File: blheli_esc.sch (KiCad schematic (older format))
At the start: 42 parts, among them J1 Conn_01x03_Male, Q1 BC847, Q2 BC847, Q3 BC847, U1 AP1509, U2 EFM8BB21F16G

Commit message: first draft complete
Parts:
- added TP6: PHASE_A, TestPoint:TestPoint_Pad_1.5x1.5mm, symbol Connector:TestPoint
- added TP7: PHASE_B, TestPoint:TestPoint_Pad_1.5x1.5mm, symbol Connector:TestPoint
- added TP8: PHASE_C, TestPoint:TestPoint_Pad_1.5x1.5mm, symbol Connector:TestPoint
- J1: footprint Connector:FanPinHeader_1x03_P2.54mm_Vertical -> Connector_PinHeader_2.54mm:PinHeader_1x03_P2.54mm_Vertical
- L1: footprint Inductor_SMD:L_12x12mm_H4.5mm -> blheli_esc:inductor_3x3mm
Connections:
- net PHASE_A: now also TP6.1
- net PHASE_B: now also TP7.1
- net PHASE_C: now also TP8.1
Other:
- moved on the sheet: J1, TP1, TP2, TP3, TP4, TP5
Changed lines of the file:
@@
 EESchema Schematic File Version 4
+LIBS:blheli_esc-cache
 EELAYER 26 0
 EELAYER END
@@
 Wire Wire Line
 	9850 1400 9850 1500
-Text GLabel 10700 1300 2    50   Output ~ 0
+Text GLabel 2850 4650 0    50   Input ~ 0
 PHASE_A
 Connection ~ 9850 1300
@@
 F 0 "L1" V 5822 1400 50  0000 C CNN
 F 1 "47uH" V 5913 1400 50  0000 C CNN
-F 2 "Inductor_SMD:L_12x12mm_H4.5mm" H 6000 1400 50  0001 C CNN
+F 2 "blheli_esc:inductor_3x3mm" H 6000 1400 50  0001 C CNN
 F 3 "~" H 6000 1400 50  0001 C CNN
 	1    6000 1400
@@
 L Connector:TestPoint TP2
 U 1 1 5C2EF43A
+P 3050 3600
+F 0 "TP2" V 3004 3787 50  0000 L CNN
+F 1 "C2CK" V 3095 3787 50  0000 L CNN
+F 2 "TestPoint:TestPoint_THTPad_D1.0mm_Drill0.5mm" H 3250 3600 50  0001 C CNN
+F 3 "~" H 3250 3600 50  0001 C CNN
+	1    3050 3600
+	0    1    1    0
+$EndComp
+Text GLabel 2850 3600 0    50   Input ~ 0
+C2CK
+Wire Wire Line
+	2850 3600 3050 3600
+$Comp
+L Connector:TestPoint TP3
+U 1 1 5C2F3D95
+P 3050 3800
+F 0 "TP3" V 3004 3987 50  0000 L CNN
+F 1 "C2D" V 3095 3987 50  0000 L CNN
+F 2 "TestPoint:TestPoint_THTPad_D1.0mm_Drill0.5mm" H 3250 3800 50  0001 C CNN
+F 3 "~" H 3250 3800 50  0001 C CNN
+	1    3050 3800
+	0    1    1    0
+$EndComp
+Text GLabel 2850 3800 0    50   Input ~ 0
+C2D
+Wire Wire Line
+	2850 3800 3050 3800
+Text GLabel 2850 4000 0    50   Input ~ 0
+TX2
+$Comp
+L Connector:TestPoint TP4
+U 1 1 5C2F885D
+P 3050 4000
+F 0 "TP4" V 3004 4188 50  0000 L CNN
+F 1 "TX2" V 3095 4188 50  0000 L CNN
+F 2 "TestPoint:TestPoint_THTPad_D1.0mm_Drill0.5mm" H 3250 4000 50  0001 C CNN
+F 3 "~" H 3250 4000 50  0001 C CNN
+	1    3050 4000
+	0    1    1    0
+$EndComp
+Wire Wire Line
+	2850 4000 3050 4000
+Text GLabel 2850 4200 0    50   Output ~ 0
+RC_IN
+$Comp
+L Connector:TestPoint TP5
+U 1 1 5C2FD85C
 P 3050 4200
-F 0 "TP2" V 3004 4387 50  0000 L CNN
-F 1 "C2CK" V 3095 4387 50  0000 L CNN
+F 0 "TP5" V 3004 4387 50  0000 L CNN
+F 1 "RC_IN" V 3095 4387 50  0000 L CNN
 F 2 "TestPoint:TestPoint_THTPad_D1.0mm_Drill0.5mm" H 3250 4200 50  0001 C CNN
 F 3 "~" H 3250 4200 50  0001 C CNN
@@
 	0    1    1    0
 $EndComp
-Text GLabel 2850 4200 0    50   Input ~ 0
-C2CK
 Wire Wire Line
 	2850 4200 3050 4200
-$Comp
-L Connector:TestPoint TP3
-U 1 1 5C2F3D95
-P 3050 4400
-F 0 "TP3" V 3004 4587 50  0000 L CNN
-F 1 "C2D" V 3095 4587 50  0000 L CNN
-F 2 "TestPoint:TestPoint_THTPad_D1.0mm_Drill0.5mm" H 3250 4400 50  0001 C CNN
-F 3 "~" H 3250 4400 50  0001 C CNN
-	1    3050 4400
-	0    1    1    0
-$EndComp
-Text GLabel 2850 4400 0    50   Input ~ 0
-C2D
-Wire Wire Line
-	2850 4400 3050 4400
-Text GLabel 2850 4600 0    50   Input ~ 0
-TX2
-$Comp
-L Connector:TestPoint TP4
-U 1 1 5C2F885D
-P 3050 4600
-F 0 "TP4" V 3004 4788 50  0000 L CNN
-F 1 "TX2" V 3095 4788 50  0000 L CNN
-F 2 "TestPoint:TestPoint_THTPad_D1.0mm_Drill0.5mm" H 3250 4600 50  0001 C CNN
-F 3 "~" H 3250 4600 50  0001 C CNN
-	1    3050 4600
-	0    1    1    0
-$EndComp
-Wire Wire Line
-	2850 4600 3050 4600
-Text GLabel 2850 4800 0    50   Output ~ 0
-RC_IN
-$Comp
-L Connector:TestPoint TP5
-U 1 1 5C2FD85C
-P 3050 4800
-F 0 "TP5" V 3004 4987 50  0000 L CNN
-F 1 "RC_IN" V 3095 4987 50  0000 L CNN
-F 2 "TestPoint:TestPoint_THTPad_D1.0mm_Drill0.5mm" H 3250 4800 50  0001 C CNN
-F 3 "~" H 3250 4800 50  0001 C CNN
-	1    3050 4800
-	0    1    1    0
-$EndComp
-Wire Wire Line
-	2850 4800 3050 4800
 $Comp
 L Connector:Conn_01x03_Male J1
 U 1 1 5C302F31
-P 1200 4400
-F 0 "J1" H 1306 4678 50  0000 C CNN
-F 1 "Conn_01x03_Male" H 1306 4587 50  0000 C CNN
-F 2 "Connector:FanPinHeader_1x03_P2.54mm_Vertical" H 1200 4400 50  0001 C CNN
-F 3 "~" H 1200 4400 50  0001 C CNN
-	1    1200 4400
+P 1200 3800
+F 0 "J1" H 1306 4078 50  0000 C CNN
+F 1 "Conn_01x03_Male" H 1306 3987 50  0000 C CNN
+F 2 "Connector_PinHeader_2.54mm:PinHeader_1x03_P2.54mm_Vertical" H 1200 3800 50  0001 C CNN
+F 3 "~" H 1200 3800 50  0001 C CNN
+	1    1200 3800
 	1    0    0    -1
 $EndComp
@@
 L power:GND #PWR0112
 U 1 1 5C30CB8C
-P 1500 4600
-F 0 "#PWR0112" H 1500 4350 50  0001 C CNN
-F 1 "GND" H 1505 4427 50  0000 C CNN
-F 2 "" H 1500 4600 50  0001 C CNN
-F 3 "" H 1500 4600 50  0001 C CNN
-	1    1500 4600
-	1    0    0    -1
-$EndComp
-Wire Wire Line
-	1400 4500 1500 4500
-Text GLabel 1600 4300 2    50   Output ~ 0
+P 1500 4000
+F 0 "#PWR0112" H 1500 3750 50  0001 C CNN
+F 1 "GND" H 1505 3827 50  0000 C CNN
+F 2 "" H 1500 4000 50  0001 C CNN
+F 3 "" H 1500 4000 50  0001 C CNN
+	1    1500 4000
+	1    0    0    -1
+$EndComp
+Wire Wire Line
+	1400 3900 1500 3900
+Text GLabel 1600 3700 2    50   Output ~ 0
 RC_IN
 Wire Wire Line
-	1400 4300 1600 4300
+	1400 3700 1600 3700
 $Comp
 L Connector:TestPoint TP1
 U 1 1 5C32EFFC
-P 1400 4400
-F 0 "TP1" V 1354 4587 50  0000 L CNN
-F 1 "SERVO_TP" V 1445 4587 50  0000 L CNN
-F 2 "TestPoint:TestPoint_THTPad_D1.0mm_Drill0.5mm" H 1600 4400 50  0001 C CNN
-F 3 "~" H 1600 4400 50  0001 C CNN
-	1    1400 4400
-	0    1    1    0
-$EndComp
-Wire Wire Line
-	1500 4600 1500 4500
+P 1400 3800
+F 0 "TP1" V 1354 3987 50  0000 L CNN
+F 1 "SERVO_TP" V 1445 3987 50  0000 L CNN
+F 2 "TestPoint:TestPoint_THTPad_D1.0mm_Drill0.5mm" H 1600 3800 50  0001 C CNN
+F 3 "~" H 1600 3800 50  0001 C CNN
+	1    1400 3800
+	0    1    1    0
+$EndComp
+Wire Wire Line
+	1500 4000 1500 3900
 $Comp
 L blheli_esc:PAD PAD1
@@
 	5700 1750 6300 1750
 Connection ~ 5700 1750
+$Comp
+L Connector:TestPoint TP6
+U 1 1 5C2CA069
+P 3050 4650
+F 0 "TP6" V 3004 4838 50  0000 L CNN
+F 1 "PHASE_A" V 3095 4838 50  0000 L CNN
+F 2 "TestPoint:TestPoint_Pad_1.5x1.5mm" H 3250 4650 50  0001 C CNN
+F 3 "~" H 3250 4650 50  0001 C CNN
+	1    3050 4650
+	0    1    1    0
+$EndComp
+Wire Wire Line
+	2850 4650 3050 4650
+Text GLabel 2850 4900 0    50   Input ~ 0
+PHASE_B
+$Comp
+L Connector:TestPoint TP7
+U 1 1 5C2D647C
+P 3050 4900
+F 0 "TP7" V 3004 5087 50  0000 L CNN
+F 1 "PHASE_B" V 3095 5087 50  0000 L CNN
+F 2 "TestPoint:TestPoint_Pad_1.5x1.5mm" H 3250 4900 50  0001 C CNN
+F 3 "~" H 3250 4900 50  0001 C CNN
+	1    3050 4900
+	0    1    1    0
+$EndComp
+Wire Wire Line
+	2850 4900 3050 4900
+Text GLabel 2850 5150 0    50   Input ~ 0
+PHASE_C
+$Comp
+L Connector:TestPoint TP8
+U 1 1 5C2DC7CE
+P 3050 5150
+F 0 "TP8" V 3004 5337 50  0000 L CNN
+F 1 "PHASE_C" V 3095 5337 50  0000 L CNN
+F 2 "TestPoint:TestPoint_Pad_1.5x1.5mm" H 3250 5150 50  0001 C CNN
+F 3 "~" H 3250 5150 50  0001 C CNN
+	1    3050 5150
+	0    1    1    0
+$EndComp
+Wire Wire Line
+	2850 5150 3050 5150
+Text GLabel 10700 1300 2    50   Output ~ 0
+PHASE_A
 $EndSCHEMATC

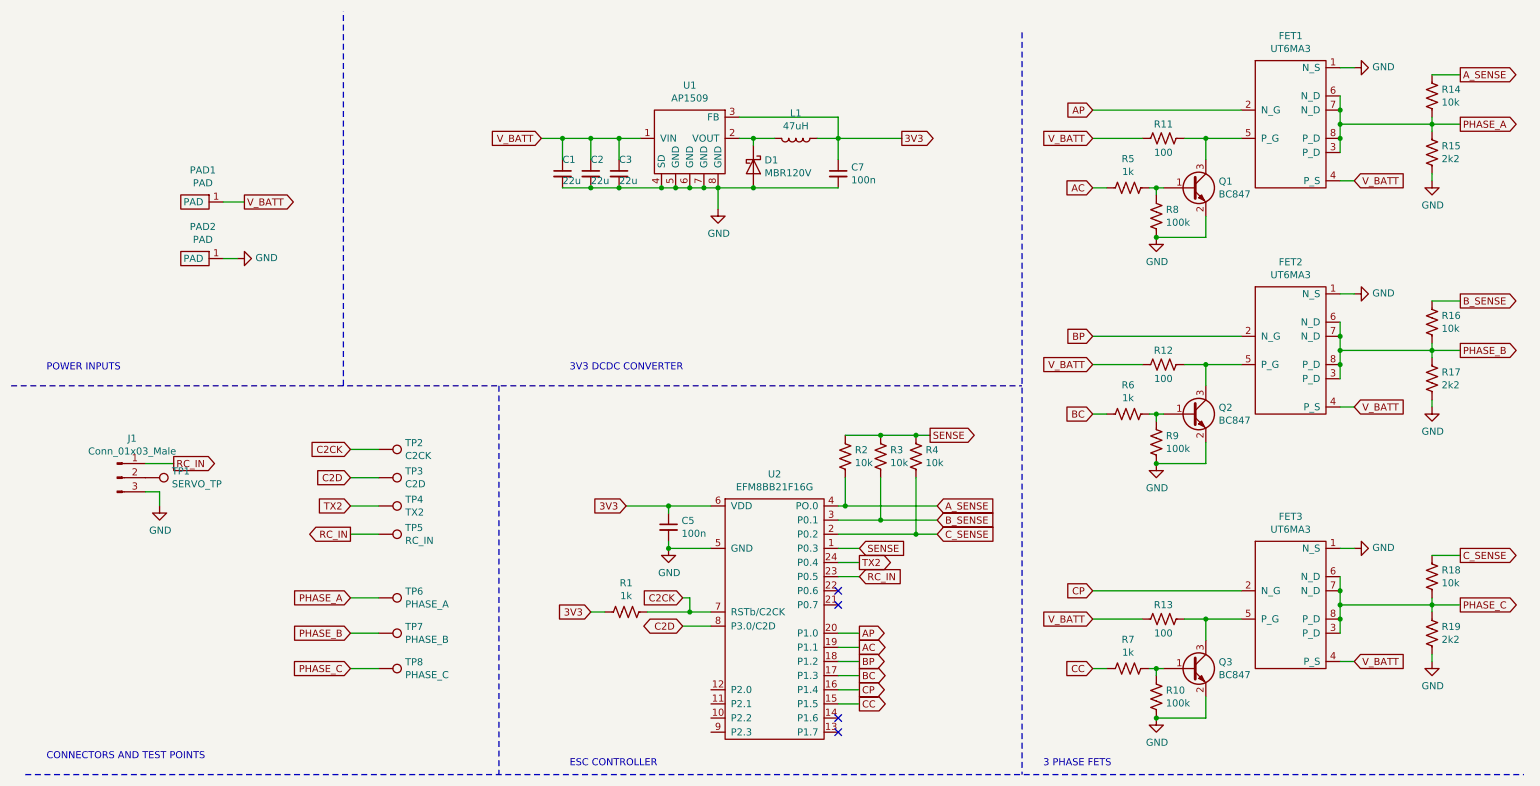
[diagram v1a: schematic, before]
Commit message: fixed voltage divider bug
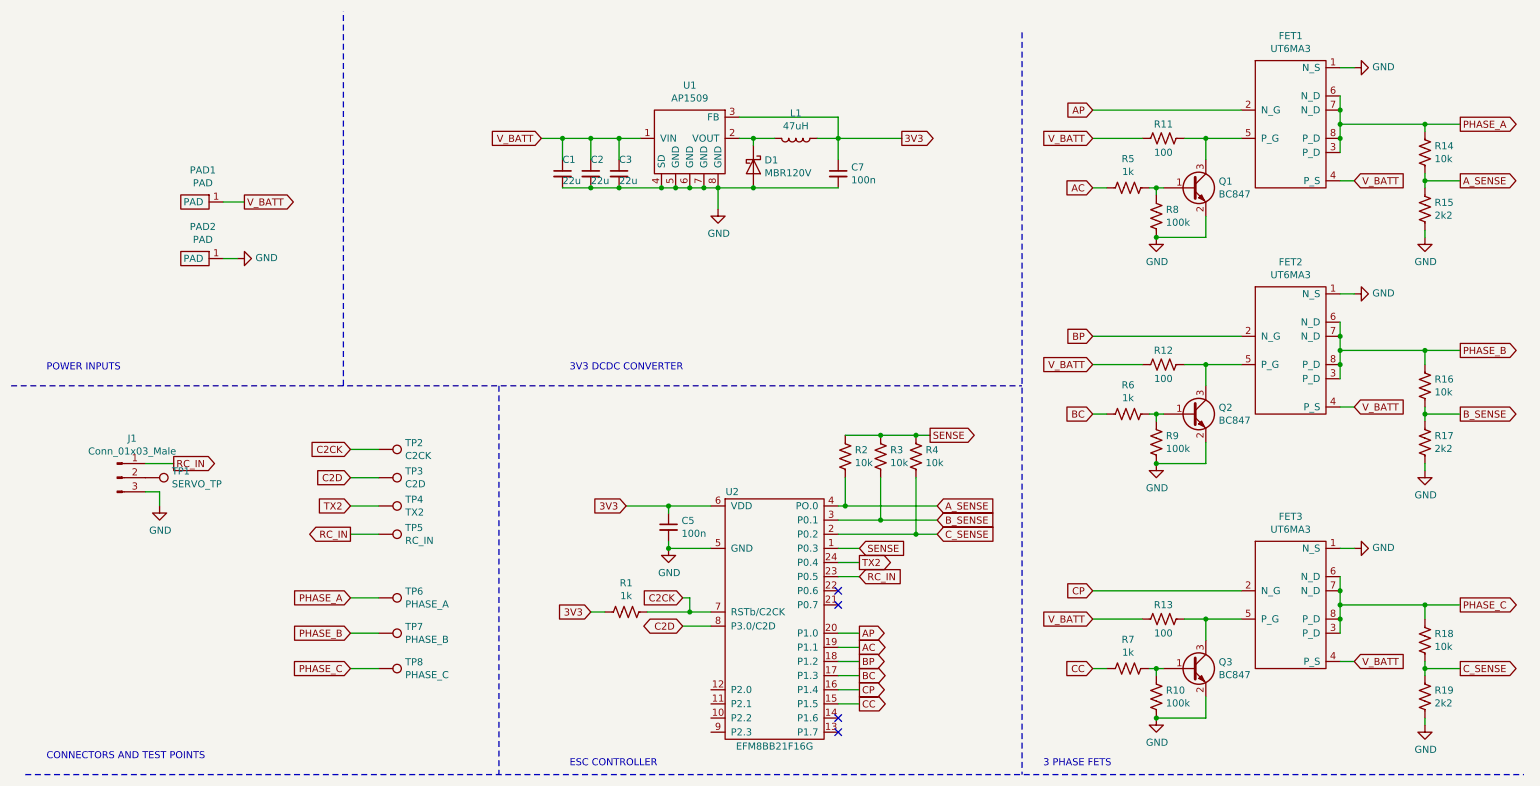
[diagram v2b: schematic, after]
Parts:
- U2: footprint Package_SO:QSOP-24_3.9x8.7mm_P0.635mm -> (none)
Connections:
- net A_SENSE: now also R14.1, R15.2; no longer R14.2
- net B_SENSE: now also R16.1, R17.2; no longer R16.2
- net C_SENSE: now also R18.1, R19.2; no longer R18.2
- net PHASE_A: now also R14.2; no longer R14.1, R15.2
- net PHASE_B: now also R16.2; no longer R16.1, R17.2
- net PHASE_C: now also R18.2; no longer R18.1, R19.2
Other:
- moved on the sheet: R14, R15, R16, R17, R18, R19
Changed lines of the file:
@@
 U 1 1 5C2A88F0
 P 5850 4800
-F 0 "U2" H 5850 5825 50  0000 C CNN
-F 1 "EFM8BB21F16G" H 5850 5734 50  0000 C CNN
-F 2 "Package_SO:QSOP-24_3.9x8.7mm_P0.635mm" H 5950 4800 50  0001 C CNN
+F 0 "U2" H 5550 5700 50  0000 C CNN
+F 1 "EFM8BB21F16G" H 5850 3900 50  0000 C CNN
+F 2 "" H 5950 4800 50  0001 C CNN
 F 3 "" H 5950 4800 50  0001 C CNN
 	1    5850 4800
@@
 L Device:R_US R15
 U 1 1 5C2AFE6A
-P 10500 1500
-F 0 "R15" H 10432 1454 50  0000 R CNN
-F 1 "2k2" H 10432 1545 50  0000 R CNN
-F 2 "Resistor_SMD:R_0603_1608Metric" V 10540 1490 50  0001 C CNN
-F 3 "~" H 10500 1500 50  0001 C CNN
-	1    10500 1500
+P 10450 1900
+F 0 "R15" H 10382 1854 50  0000 R CNN
+F 1 "2k2" H 10382 1945 50  0000 R CNN
+F 2 "Resistor_SMD:R_0603_1608Metric" V 10490 1890 50  0001 C CNN
+F 3 "~" H 10450 1900 50  0001 C CNN
+	1    10450 1900
 	-1   0    0    1
 $EndComp
@@
 L Device:R_US R14
 U 1 1 5C2AFEDE
-P 10500 1100
-F 0 "R14" H 10432 1054 50  0000 R CNN
-F 1 "10k" H 10432 1145 50  0000 R CNN
-F 2 "Resistor_SMD:R_0603_1608Metric" V 10540 1090 50  0001 C CNN
-F 3 "~" H 10500 1100 50  0001 C CNN
-	1    10500 1100
-	-1   0    0    1
-$EndComp
-Wire Wire Line
-	9850 1300 10500 1300
-Wire Wire Line
-	10500 1350 10500 1300
-Connection ~ 10500 1300
-Wire Wire Line
-	10500 1300 10700 1300
-Wire Wire Line
-	10500 1300 10500 1250
-Text GLabel 10700 950  2    50   Output ~ 0
+P 10450 1500
+F 0 "R14" H 10382 1454 50  0000 R CNN
+F 1 "10k" H 10382 1545 50  0000 R CNN
+F 2 "Resistor_SMD:R_0603_1608Metric" V 10490 1490 50  0001 C CNN
+F 3 "~" H 10450 1500 50  0001 C CNN
+	1    10450 1500
+	-1   0    0    1
+$EndComp
+Text GLabel 10700 1700 2    50   Output ~ 0
 A_SENSE
-Wire Wire Line
-	10500 950  10700 950
 $Comp
 L power:GND #PWR0104
 U 1 1 5C2B1F88
-P 10500 1700
-F 0 "#PWR0104" H 10500 1450 50  0001 C CNN
-F 1 "GND" H 10505 1527 50  0000 C CNN
-F 2 "" H 10500 1700 50  0001 C CNN
-F 3 "" H 10500 1700 50  0001 C CNN
-	1    10500 1700
-	1    0    0    -1
-$EndComp
-Wire Wire Line
-	10500 1700 10500 1650
+P 10450 2100
+F 0 "#PWR0104" H 10450 1850 50  0001 C CNN
+F 1 "GND" H 10455 1927 50  0000 C CNN
+F 2 "" H 10450 2100 50  0001 C CNN
+F 3 "" H 10450 2100 50  0001 C CNN
+	1    10450 2100
+	1    0    0    -1
+$EndComp
+Wire Wire Line
+	10450 2100 10450 2050
 $Comp
 L Device:R_US R2
@@
 L Device:R_US R17
 U 1 1 5C2BCC33
-P 10500 3100
-F 0 "R17" H 10432 3054 50  0000 R CNN
-F 1 "2k2" H 10432 3145 50  0000 R CNN
-F 2 "Resistor_SMD:R_0603_1608Metric" V 10540 3090 50  0001 C CNN
-F 3 "~" H 10500 3100 50  0001 C CNN
-	1    10500 3100
+P 10450 3550
+F 0 "R17" H 10382 3504 50  0000 R CNN
+F 1 "2k2" H 10382 3595 50  0000 R CNN
+F 2 "Resistor_SMD:R_0603_1608Metric" V 10490 3540 50  0001 C CNN
+F 3 "~" H 10450 3550 50  0001 C CNN
+	1    10450 3550
 	-1   0    0    1
 $EndComp
@@
 L Device:R_US R16
 U 1 1 5C2BCC39
-P 10500 2700
-F 0 "R16" H 10432 2654 50  0000 R CNN
-F 1 "10k" H 10432 2745 50  0000 R CNN
-F 2 "Resistor_SMD:R_0603_1608Metric" V 10540 2690 50  0001 C CNN
-F 3 "~" H 10500 2700 50  0001 C CNN
-	1    10500 2700
-	-1   0    0    1
-$EndComp
-Wire Wire Line
-	9850 2900 10500 2900
-Wire Wire Line
-	10500 2950 10500 2900
-Connection ~ 10500 2900
-Wire Wire Line
-	10500 2900 10700 2900
-Wire Wire Line
-	10500 2900 10500 2850
-Text GLabel 10700 2550 2    50   Output ~ 0
+P 10450 3150
+F 0 "R16" H 10382 3104 50  0000 R CNN
+F 1 "10k" H 10382 3195 50  0000 R CNN
+F 2 "Resistor_SMD:R_0603_1608Metric" V 10490 3140 50  0001 C CNN
+F 3 "~" H 10450 3150 50  0001 C CNN
+	1    10450 3150
+	-1   0    0    1
+$EndComp
+Text GLabel 10700 3350 2    50   Output ~ 0
 B_SENSE
-Wire Wire Line
-	10500 2550 10700 2550
 $Comp
 L power:GND #PWR0107
 U 1 1 5C2BCC46
-P 10500 3300
-F 0 "#PWR0107" H 10500 3050 50  0001 C CNN
-F 1 "GND" H 10505 3127 50  0000 C CNN
-F 2 "" H 10500 3300 50  0001 C CNN
-F 3 "" H 10500 3300 50  0001 C CNN
-	1    10500 3300
-	1    0    0    -1
-$EndComp
-Wire Wire Line
-	10500 3300 10500 3250
+P 10450 3750
+F 0 "#PWR0107" H 10450 3500 50  0001 C CNN
+F 1 "GND" H 10455 3577 50  0000 C CNN
+F 2 "" H 10450 3750 50  0001 C CNN
+F 3 "" H 10450 3750 50  0001 C CNN
+	1    10450 3750
+	1    0    0    -1
+$EndComp
+Wire Wire Line
+	10450 3750 10450 3700
 $Comp
 L Transistor_BJT:BC847 Q3
@@
 L Device:R_US R19
 U 1 1 5C2BFE26
-P 10500 4900
-F 0 "R19" H 10432 4854 50  0000 R CNN
-F 1 "2k2" H 10432 4945 50  0000 R CNN
-F 2 "Resistor_SMD:R_0603_1608Metric" V 10540 4890 50  0001 C CNN
-F 3 "~" H 10500 4900 50  0001 C CNN
-	1    10500 4900
+P 10450 5350
+F 0 "R19" H 10382 5304 50  0000 R CNN
+F 1 "2k2" H 10382 5395 50  0000 R CNN
+F 2 "Resistor_SMD:R_0603_1608Metric" V 10490 5340 50  0001 C CNN
+F 3 "~" H 10450 5350 50  0001 C CNN
+	1    10450 5350
 	-1   0    0    1
 $EndComp
@@
 L Device:R_US R18
 U 1 1 5C2BFE2C
-P 10500 4500
-F 0 "R18" H 10432 4454 50  0000 R CNN
-F 1 "10k" H 10432 4545 50  0000 R CNN
-F 2 "Resistor_SMD:R_0603_1608Metric" V 10540 4490 50  0001 C CNN
-F 3 "~" H 10500 4500 50  0001 C CNN
-	1    10500 4500
-	-1   0    0    1
-$EndComp
-Wire Wire Line
-	9850 4700 10500 4700
-Wire Wire Line
-	10500 4750 10500 4700
-Connection ~ 10500 4700
-Wire Wire Line
-	10500 4700 10700 4700
-Wire Wire Line
-	10500 4700 10500 4650
-Text GLabel 10700 4350 2    50   Output ~ 0
+P 10450 4950
+F 0 "R18" H 10382 4904 50  0000 R CNN
+F 1 "10k" H 10382 4995 50  0000 R CNN
+F 2 "Resistor_SMD:R_0603_1608Metric" V 10490 4940 50  0001 C CNN
+F 3 "~" H 10450 4950 50  0001 C CNN
+	1    10450 4950
+	-1   0    0    1
+$EndComp
+Text GLabel 10700 5150 2    50   Output ~ 0
 C_SENSE
-Wire Wire Line
-	10500 4350 10700 4350
 $Comp
 L power:GND #PWR0110
 U 1 1 5C2BFE39
-P 10500 5100
-F 0 "#PWR0110" H 10500 4850 50  0001 C CNN
-F 1 "GND" H 10505 4927 50  0000 C CNN
-F 2 "" H 10500 5100 50  0001 C CNN
-F 3 "" H 10500 5100 50  0001 C CNN
-	1    10500 5100
-	1    0    0    -1
-$EndComp
-Wire Wire Line
-	10500 5100 10500 5050
+P 10450 5550
+F 0 "#PWR0110" H 10450 5300 50  0001 C CNN
+F 1 "GND" H 10455 5377 50  0000 C CNN
+F 2 "" H 10450 5550 50  0001 C CNN
+F 3 "" H 10450 5550 50  0001 C CNN
+	1    10450 5550
+	1    0    0    -1
+$EndComp
+Wire Wire Line
+	10450 5550 10450 5500
 $Comp
 L blheli_esc:AP1509 U1
@@
 Text GLabel 10700 1300 2    50   Output ~ 0
 PHASE_A
+Wire Wire Line
+	9850 1300 10450 1300
+Wire Wire Line
+	10450 1350 10450 1300
+Connection ~ 10450 1300
+Wire Wire Line
+	10450 1300 10700 1300
+Wire Wire Line
+	10450 1650 10450 1700
+Wire Wire Line
+	10450 1700 10700 1700
+Connection ~ 10450 1700
+Wire Wire Line
+	10450 1700 10450 1750
+Wire Wire Line
+	9850 2900 10450 2900
+Wire Wire Line
+	10450 3000 10450 2900
+Connection ~ 10450 2900
+Wire Wire Line
+	10450 2900 10700 2900
+Wire Wire Line
+	10450 3300 10450 3350
+Wire Wire Line
+	10450 3350 10700 3350
+Connection ~ 10450 3350
+Wire Wire Line
+	10450 3350 10450 3400
+Wire Wire Line
+	9850 4700 10450 4700
+Wire Wire Line
+	10450 4800 10450 4700
+Connection ~ 10450 4700
+Wire Wire Line
+	10450 4700 10700 4700
+Wire Wire Line
+	10450 5100 10450 5150
+Wire Wire Line
+	10450 5150 10700 5150
+Connection ~ 10450 5150
+Wire Wire Line
+	10450 5150 10450 5200
 $EndSCHEMATC
